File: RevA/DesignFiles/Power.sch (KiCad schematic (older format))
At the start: 0 parts

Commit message: placed power block and usb connector
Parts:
- added C101: 10uF, symbol C
- added C102: 100nF, symbol C
- added J101: USB_OTG, symbol USB_OTG
- added R101: 100, symbol R
- added U1: ICE40HX1K-TQ144, symbol ICE40HX1K-TQ144
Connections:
- new net: C101.1, C102.1, R101.1, U1.35 (PLLGND), U1.36 (PLLVCC)
- new net +1V2: R101.2, U1.111 (VCC_04), U1.27 (VCC_02), U1.51 (VCC_01), U1.92 (VCC_03)
- new net +5V: J101.1 (VCC)
- new net GND: C101.2, C102.2, J101.5 (GND), J101.6 (shield), U1.103 (GND_07), U1.13 (GND_02), U1.132 (GND_08), U1.14 (GND_03), U1.140 (GND_09), U1.5 (GND_01), U1.59 (GND_04), U1.69 (GND_05), U1.86 (GND_06)
- no-connect marks 0 -> 5
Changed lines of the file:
@@
 Comment4 ""
 $EndDescr
+$Comp
+L ICE40HX1K-TQ144 U1
+U 1 1 57FD4F6E
+P 2600 1750
+F 0 "U1" H 2900 1900 60  0000 C CNN
+F 1 "ICE40HX1K-TQ144" H 3250 1800 60  0000 C CNN
+F 2 "" H 2600 1000 60  0000 C CNN
+F 3 "" H 2600 1000 60  0000 C CNN
+	1    2600 1750
+	1    0    0    -1
+$EndComp
+Wire Wire Line
+	2550 1800 2550 2650
+Wire Wire Line
+	2550 1800 2600 1800
+Wire Wire Line
+	2600 1900 2550 1900
+Connection ~ 2550 1900
+Wire Wire Line
+	2600 2000 2550 2000
+Connection ~ 2550 2000
+Wire Wire Line
+	2600 2100 2550 2100
+Connection ~ 2550 2100
+Wire Wire Line
+	2600 2200 2550 2200
+Connection ~ 2550 2200
+Wire Wire Line
+	2600 2300 2550 2300
+Connection ~ 2550 2300
+Wire Wire Line
+	2600 2400 2550 2400
+Connection ~ 2550 2400
+Wire Wire Line
+	2600 2500 2550 2500
+Connection ~ 2550 2500
+Connection ~ 2550 2600
+$Comp
+L C C102
+U 1 1 57FD5309
+P 2400 3100
+F 0 "C102" H 2425 3200 50  0000 L CNN
+F 1 "100nF" H 2425 3000 50  0000 L CNN
+F 2 "" H 2438 2950 50  0000 C CNN
+F 3 "" H 2400 3100 50  0000 C CNN
+	1    2400 3100
+	1    0    0    -1
+$EndComp
+$Comp
+L C C101
+U 1 1 57FD534A
+P 2000 3100
+F 0 "C101" H 2025 3200 50  0000 L CNN
+F 1 "10uF" H 2025 3000 50  0000 L CNN
+F 2 "" H 2038 2950 50  0000 C CNN
+F 3 "" H 2000 3100 50  0000 C CNN
+	1    2000 3100
+	1    0    0    -1
+$EndComp
+$Comp
+L R R101
+U 1 1 57FD5387
+P 2000 2600
+F 0 "R101" H 2100 2550 50  0000 L CNN
+F 1 "100" H 2150 2650 50  0000 L CNN
+F 2 "" V 1930 2600 50  0000 C CNN
+F 3 "" H 2000 2600 50  0000 C CNN
+	1    2000 2600
+	-1   0    0    1
+$EndComp
+$Comp
+L +1V2 #PWR?
+U 1 1 57FD53CA
+P 2000 2400
+F 0 "#PWR?" H 2000 2250 50  0001 C CNN
+F 1 "+1V2" H 2000 2540 50  0000 C CNN
+F 2 "" H 2000 2400 50  0000 C CNN
+F 3 "" H 2000 2400 50  0000 C CNN
+	1    2000 2400
+	1    0    0    -1
+$EndComp
+Wire Wire Line
+	2400 2800 2400 2950
+Wire Wire Line
+	2400 3300 2400 3250
+Connection ~ 2000 3300
+Wire Wire Line
+	2600 2600 2550 2600
+Wire Wire Line
+	2000 2800 2600 2800
+Connection ~ 2400 2800
+Wire Wire Line
+	2600 2900 2550 2900
+Wire Wire Line
+	2550 2900 2550 2800
+Connection ~ 2550 2800
+Wire Wire Line
+	2000 2450 2000 2400
+$Comp
+L +1V2 #PWR?
+U 1 1 57FD5AF7
+P 4850 2550
+F 0 "#PWR?" H 4850 2400 50  0001 C CNN
+F 1 "+1V2" H 4850 2690 50  0000 C CNN
+F 2 "" H 4850 2550 50  0000 C CNN
+F 3 "" H 4850 2550 50  0000 C CNN
+	1    4850 2550
+	1    0    0    -1
+$EndComp
+Wire Wire Line
+	4850 2900 4850 2550
+Connection ~ 4850 2800
+Connection ~ 4850 2700
+Connection ~ 4850 2600
+NoConn ~ 4650 2450
+NoConn ~ 4650 2350
+NoConn ~ 4650 2250
+NoConn ~ 4650 2150
+NoConn ~ 4650 2050
+Wire Wire Line
+	2000 2750 2000 2950
+Connection ~ 2000 2800
+Wire Wire Line
+	2000 3250 2000 3350
+Wire Wire Line
+	2000 3300 2400 3300
+Wire Wire Line
+	4850 2900 4650 2900
+Wire Wire Line
+	4650 2800 4850 2800
+Wire Wire Line
+	4650 2700 4850 2700
+Wire Wire Line
+	4650 2600 4850 2600
+$Comp
+L USB_OTG J101
+U 1 1 57FD6473
+P 1850 5500
+F 0 "J101" V 1650 5700 50  0000 L CNN
+F 1 "USB_OTG" V 1750 5700 50  0000 L CNN
+F 2 "" V 1800 5400 50  0000 C CNN
+F 3 "" V 1800 5400 50  0000 C CNN
+	1    1850 5500
+	0    1    1    0
+$EndComp
+Wire Wire Line
+	1500 5700 1550 5700
+Wire Wire Line
+	1950 5900 1950 5950
+Wire Wire Line
+	1950 5950 1500 5950
+Connection ~ 1500 5950
+Wire Wire Line
+	1500 6000 1500 5700
+$Comp
+L +5V #PWR?
+U 1 1 57FD6B2E
+P 1500 5250
+F 0 "#PWR?" H 1500 5100 50  0001 C CNN
+F 1 "+5V" H 1500 5390 50  0000 C CNN
+F 2 "" H 1500 5250 50  0000 C CNN
+F 3 "" H 1500 5250 50  0000 C CNN
+	1    1500 5250
+	1    0    0    -1
+$EndComp
+Wire Wire Line
+	1550 5300 1500 5300
+Wire Wire Line
+	1500 5300 1500 5250
+$Comp
+L GND #PWR?
+U 1 1 57FD6D3C
+P 2000 3350
+F 0 "#PWR?" H 2000 3100 50  0001 C CNN
+F 1 "GND" H 2000 3200 50  0001 C CNN
+F 2 "" H 2000 3350 50  0000 C CNN
+F 3 "" H 2000 3350 50  0000 C CNN
+	1    2000 3350
+	1    0    0    -1
+$EndComp
+$Comp
+L GND #PWR?
+U 1 1 57FD6DBE
+P 2550 2650
+F 0 "#PWR?" H 2550 2400 50  0001 C CNN
+F 1 "GND" H 2550 2500 50  0001 C CNN
+F 2 "" H 2550 2650 50  0000 C CNN
+F 3 "" H 2550 2650 50  0000 C CNN
+	1    2550 2650
+	1    0    0    -1
+$EndComp
+$Comp
+L GND #PWR?
+U 1 1 57FD6E3C
+P 1500 6000
+F 0 "#PWR?" H 1500 5750 50  0001 C CNN
+F 1 "GND" H 1500 5850 50  0001 C CNN
+F 2 "" H 1500 6000 50  0000 C CNN
+F 3 "" H 1500 6000 50  0000 C CNN
+	1    1500 6000
+	1    0    0    -1
+$EndComp
 $EndSCHEMATC

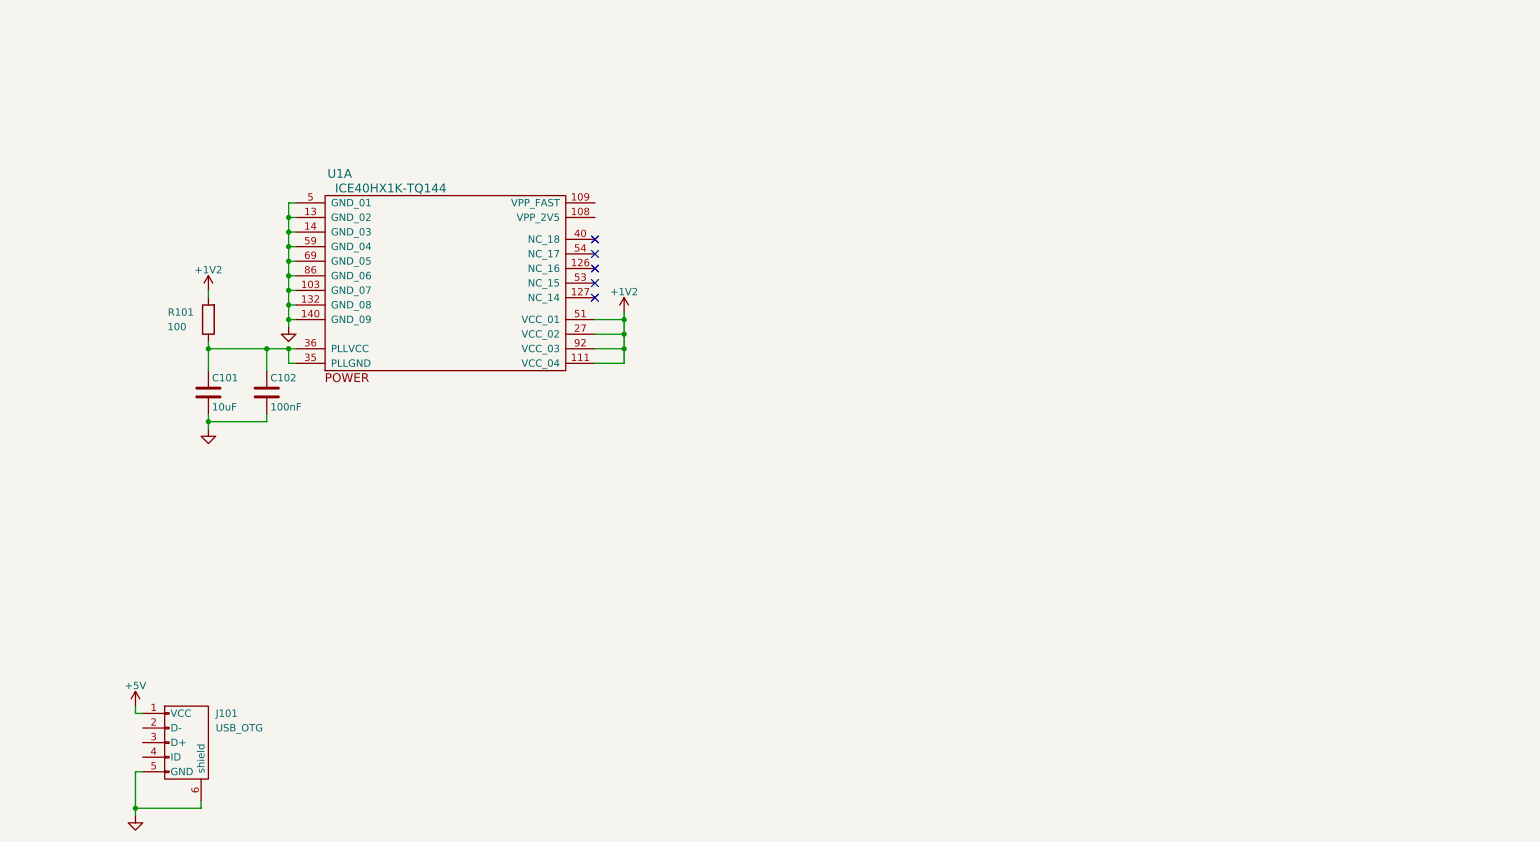
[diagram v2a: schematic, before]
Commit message: reg add to power
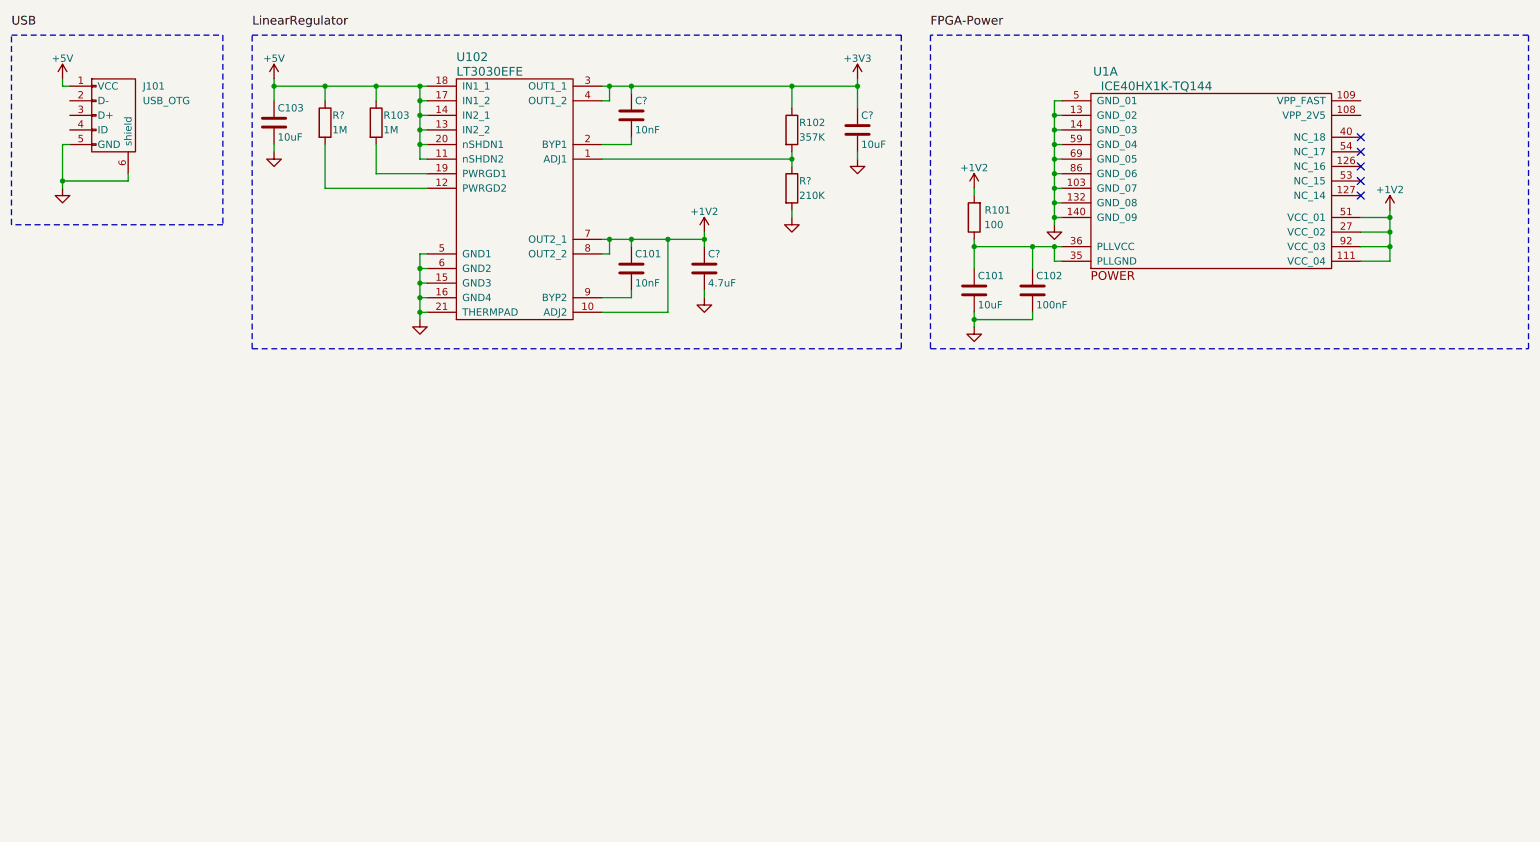
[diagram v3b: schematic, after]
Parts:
- added C101, C?: 10nF, symbol C
- added C103, C?: 10uF, symbol C
- added C?: 4.7uF, symbol C
- added R102: 357K, symbol R
- added R103, R?: 1M, symbol R
- added R?: 210K, symbol R
- added U102: LT3030EFE, symbol LT3030EFE
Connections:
- net +1V2: now also C101.1, C?.1, U102.10 (ADJ2), U102.7 (OUT2_1), U102.8 (OUT2_2)
- net +5V: now also C103.1, R103.1, R?.1, U102.11 (nSHDN2), U102.13 (IN2_2), U102.14 (IN2_1), U102.17 (IN1_2), U102.18 (IN1_1), U102.20 (nSHDN1)
- net GND: now also C103.2, C?.2, C?.2, R?.2, U102.15 (GND3), U102.16 (GND4), U102.21 (THERMPAD), U102.5 (GND1), U102.6 (GND2)
- new net: R102.2, R?.1, U102.1 (ADJ1)
- new net: R?.2, U102.12 (PWRGD2)
- new net: R103.2, U102.19 (PWRGD1)
- new net: C?.2, U102.2 (BYP1)
- new net: C101.2, U102.9 (BYP2)
- new net +3V3: C?.1, C?.1, R102.1, U102.3 (OUT1_1), U102.4 (OUT1_2)
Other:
- moved on the sheet: C101, C102, J101, R101, U1A
